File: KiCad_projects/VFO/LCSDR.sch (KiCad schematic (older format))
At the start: 78 parts, among them J1 SPI, J10 ENCODER, J11 LCD, J12 keyboard, J2 BAND, J3 OUT-TX, J4 UART, J5 PA, J6 12v, J7 OUT 1-120Mhz, J8 ATT, J9 PRE, Q1 MMBT2907, Q2 MMBT2222, Q3 MMBT2907, U1 ATMEGA328P-AU, U2 Si5351, U3 PCA9306, U4 ADuM1201BR, U5 LD1117S50TR, U6 LD1117S33TR, Y1 16Mhz, Y2 25Mhz

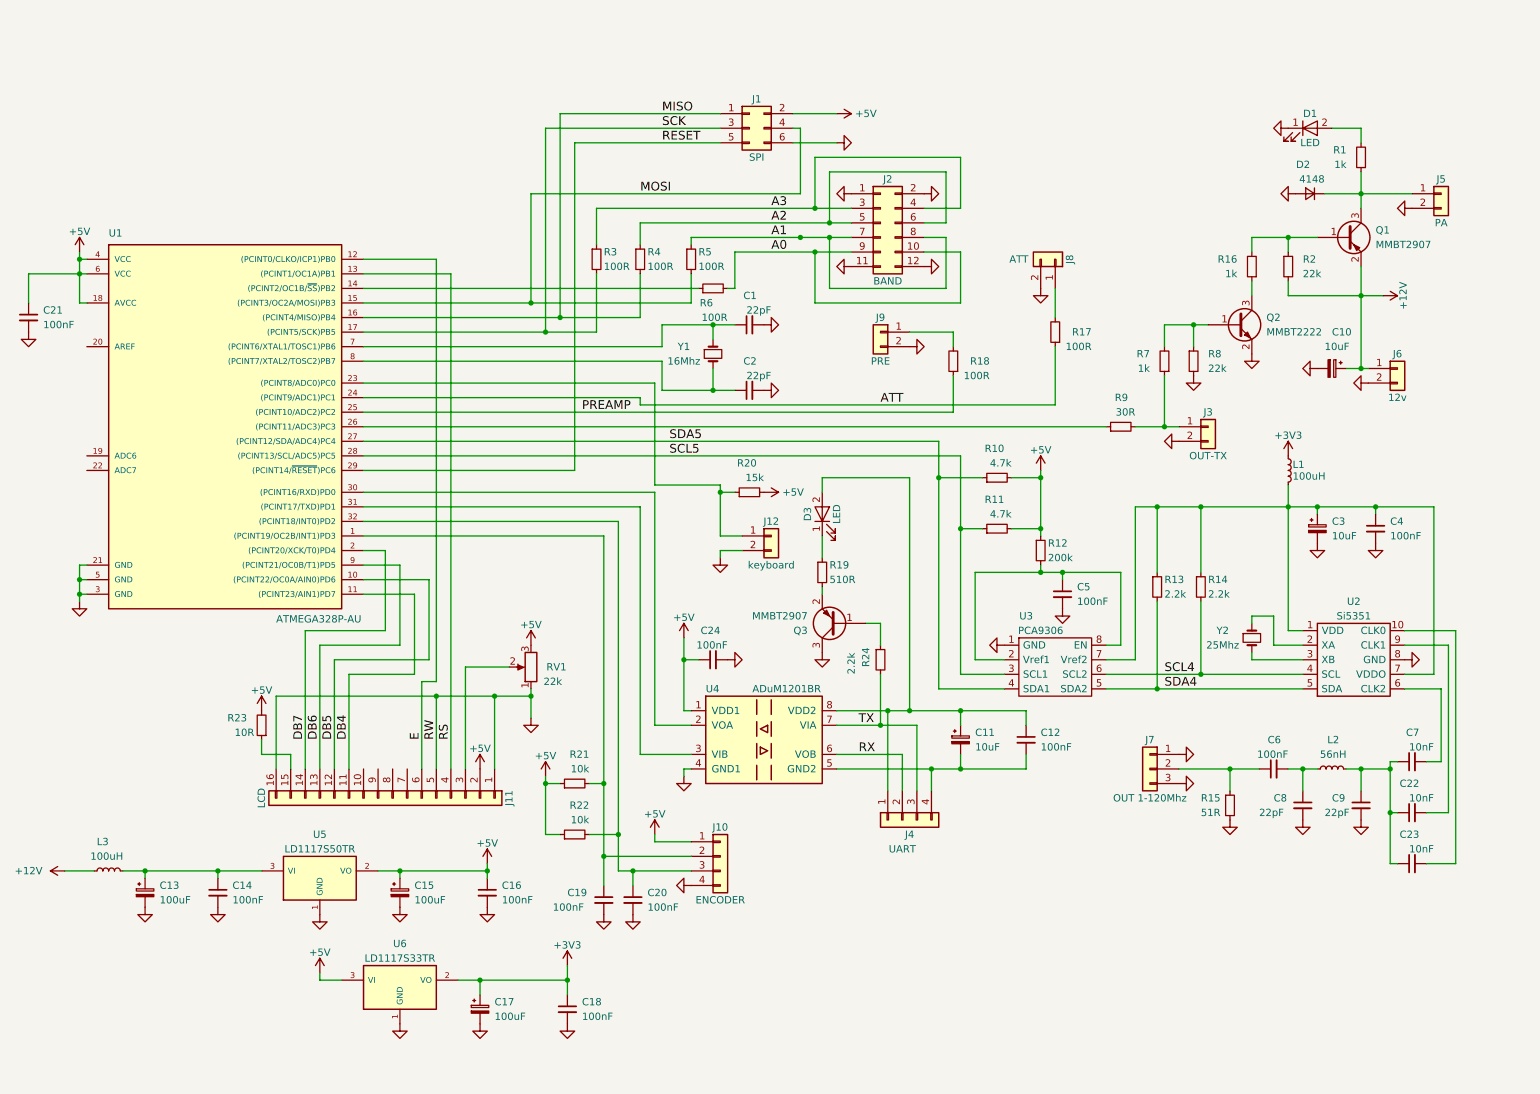
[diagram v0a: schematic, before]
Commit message: modified VFO schematics and PCB. clk0/clk1/clk2, unified management board
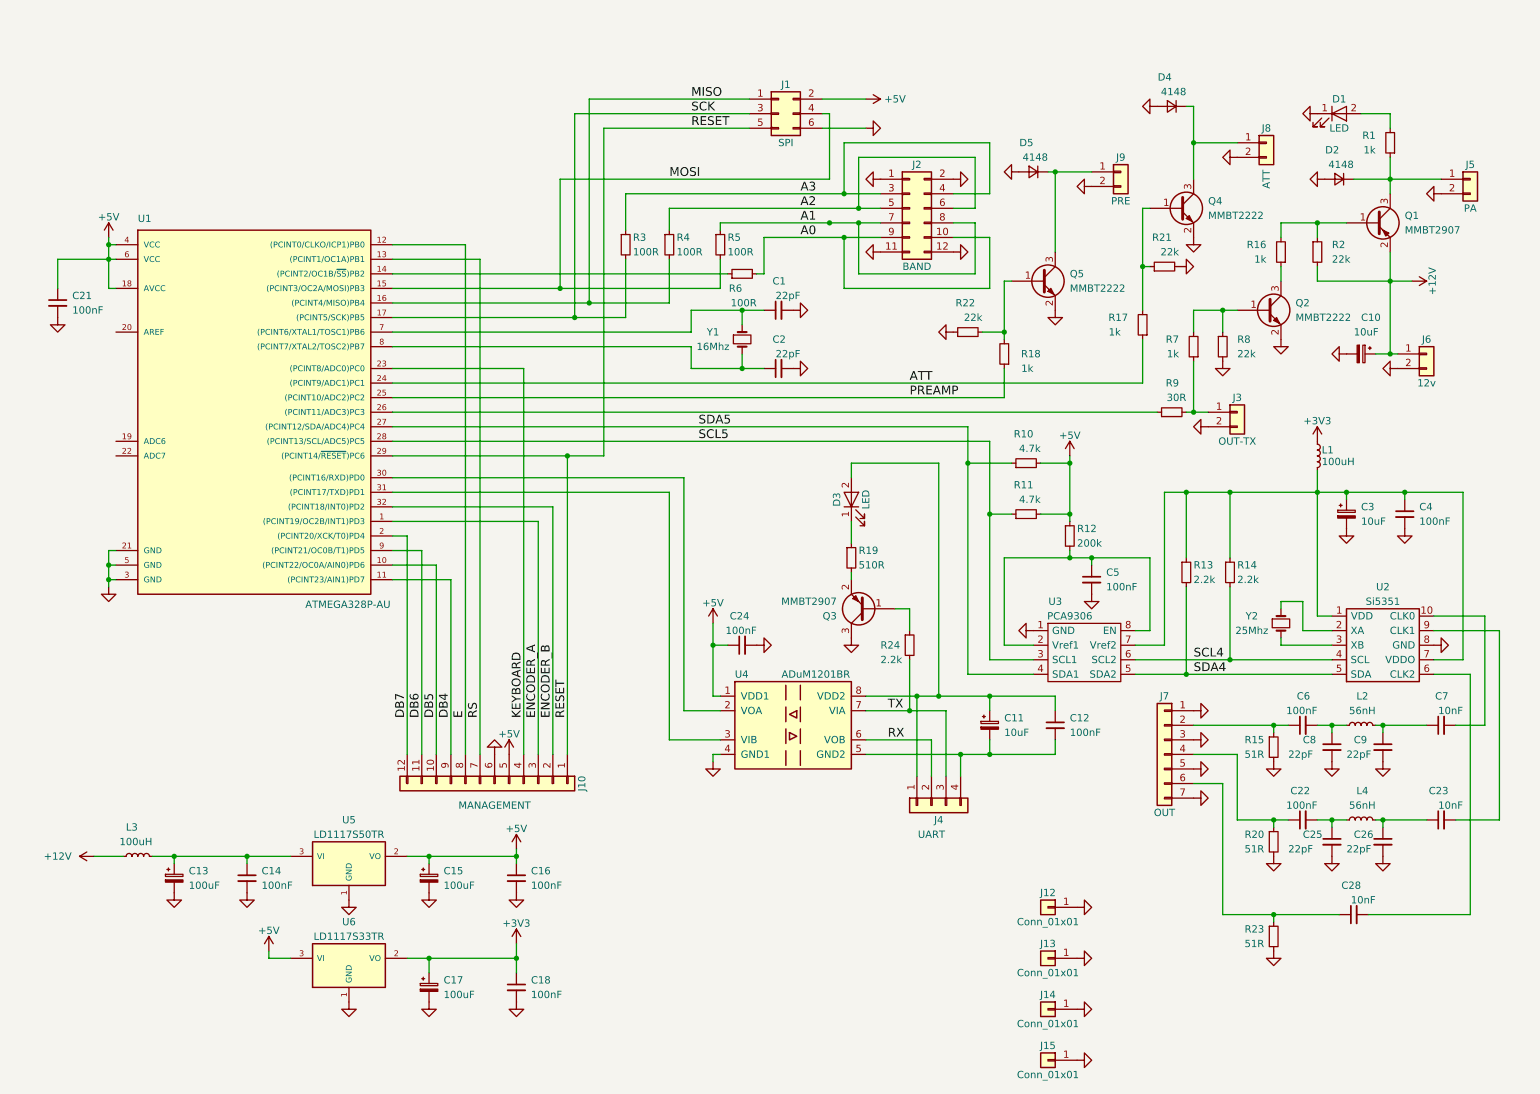
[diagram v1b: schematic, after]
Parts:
- removed C19, C20: 100nF, LCSDR:C_1206_0603, symbol C_Small
- removed J10: ENCODER, Pin_Headers:Pin_Header_Angled_1x04_Pitch2.54mm, symbol Conn_01x04
- removed J11: LCD, Pin_Headers:Pin_Header_Angled_1x16_Pitch2.54mm, symbol Conn_01x16
- removed J12: keyboard, Pin_Headers:Pin_Header_Angled_1x02_Pitch2.54mm, symbol Conn_01x02
- removed J7: OUT 1-120Mhz, Pin_Headers:Pin_Header_Straight_1x03_Pitch2.54mm, symbol Conn_01x03
- removed RV1: 22k, Potentiometers:Potentiometer_Trimmer_Piher_PT-6v_Horizontal, symbol POT
- added C25, C26: 22pF, LCSDR:C_1206_0603, symbol C_Small
- added C28: 10nF, LCSDR:C_1206_0603, symbol C_Small
- added D4, D5: 4148, Diodes_SMD:D_MiniMELF_Handsoldering, symbol D_Small
- added J10: MANAGEMENT, Pin_Headers:Pin_Header_Angled_1x12_Pitch2.54mm, symbol Conn_01x12
- added J12, J13, J14, J15: Conn_01x01, Mounting_Holes:MountingHole_3.2mm_M3_DIN965_Pad, symbol Conn_01x01
- added J7: OUT, Pin_Headers:Pin_Header_Straight_1x07_Pitch2.54mm, symbol Conn_01x07
- added L4: 56nH, LCSDR:C_1206_0603, symbol L_Small
- added Q4, Q5: MMBT2222, TO_SOT_Packages_SMD:SOT-23W_Handsoldering, symbol Q_NPN_BEC
- C22: value 10nF -> 100nF
- L2: footprint Capacitors_SMD:C_0603_HandSoldering -> LCSDR:C_1206_0603
- R17, R18: value 100R -> 1k
- R20: value 15k -> 51R
- R21, R22: value 10k -> 22k
- R23: value 10R -> 51R
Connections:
- net +5V: now also J10.5 (Pin_5); no longer R20.2, R21.1, R22.1, R23.2
- net DB4: now also J10.9 (Pin_9)
- net DB5: now also J10.10 (Pin_10)
- net DB6: now also J10.11 (Pin_11)
- net DB7: now also J10.12 (Pin_12)
- net E: now also J10.8 (Pin_8)
- net GND: now also R20.2, R21.2, R22.1, R23.2, C25.2, C26.2, D4.2 (A), D5.2 (A), J10.6 (Pin_6), J12.1 (Pin_1), J13.1 (Pin_1), J14.1 (Pin_1), J15.1 (Pin_1), J7.1 (Pin_1), J7.3 (Pin_3), J7.5 (Pin_5), J7.7 (Pin_7), Q4.2 (E), Q5.2 (E)
- net RESET: now also J10.1 (Pin_1)
- net RS: now also J10.7 (Pin_7)
- net ENCODER_A: now reaches U1.1 ((PCINT19/OC2B/INT1)PD3)
- net ENCODER_A: now also J10.3 (Pin_3); no longer R21.2
- net at R20.1: now also C22.1, J7.4 (Pin_4); no longer U1.23 ((PCINT8/ADC0)PC0)
- net at R22.2: now also R18.2, Q5.1 (B); no longer U1.32 ((PCINT18/INT0)PD2)
- net at U2.10 (CLK0): now also C7.2; no longer C23.2
- net at U2.6 (CLK2): now also C28.2; no longer C7.2
- net at U2.9 (CLK1): now also C23.2; no longer C22.2
- net at C7.1, C9.1, L2.2: no longer C22.1, C23.1
- net at C6.1, R15.1: now also J7.2 (Pin_2)
- net at R23.1: now also C28.1, J7.6 (Pin_6)
- net at J9.1 (Pin_1): now also D5.1 (K), Q5.3 (C); no longer R18.2
- net at R17.2: now also R21.1, Q4.1 (B); no longer J8.1 (Pin_1)
- new net: D4.1 (K), J8.1 (Pin_1), Q4.3 (C)
- new net: C23.1, C26.1, L4.2
- new net: C22.2, C25.1, L4.1
- new net ENCODER_B: J10.2 (Pin_2), U1.32 ((PCINT18/INT0)PD2)
- new net KEYBOARD: J10.4 (Pin_4), U1.23 ((PCINT8/ADC0)PC0)
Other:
- moved on the sheet: C1, C10, C11, C12, C13, C14, C15, C16, C17, C18, C2, C21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

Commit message: Separate boards for VFO, CLK0, CLK1, CLK2 and SWR
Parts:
- added C19, C20: 100nF, LCSDR:C_1206_0603, symbol C_Small
- added J11: Conn_01x03, Pin_Headers:Pin_Header_Angled_1x03_Pitch2.54mm, symbol Conn_01x03
- added R25, R26, R27, R28: 2.2k, LCSDR:R_1206_0603, symbol R_Small
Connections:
- net GND: now also C19.1, C20.1, J11.3 (Pin_3), R25.2, R26.2
- net at U1.19 (ADC6): now also C19.2, R25.1, R28.1
- net at U1.22 (ADC7): now also C20.2, R26.1, R27.1
- new net: J11.1 (Pin_1), R28.2
- new net: J11.2 (Pin_2), R27.2
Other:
- moved on the sheet: C1, C10, C11, C12, C13, C14, C15, C16, C17, C18, C2, C21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

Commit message: Fix some small issues and first tantal release
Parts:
- C10, C11, C3: footprint Capacitors_ThroughHole:CP_Radial_D5.0mm_P2.00mm -> Capacitors_Tantalum_SMD:CP_Tantalum_Case-A_EIA-3216-18_Hand
- C13, C15, C17: footprint Capacitors_ThroughHole:CP_Radial_D6.3mm_P2.50mm -> Capacitors_Tantalum_SMD:CP_Tantalum_Case-D_EIA-7343-31_Hand

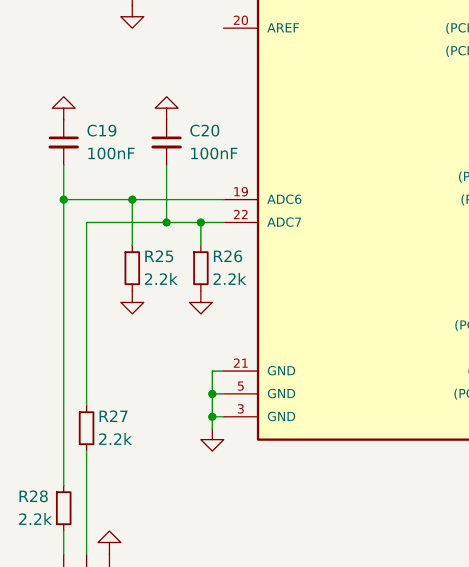
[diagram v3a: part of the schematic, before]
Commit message: Fix Issues with PCB Silk Text
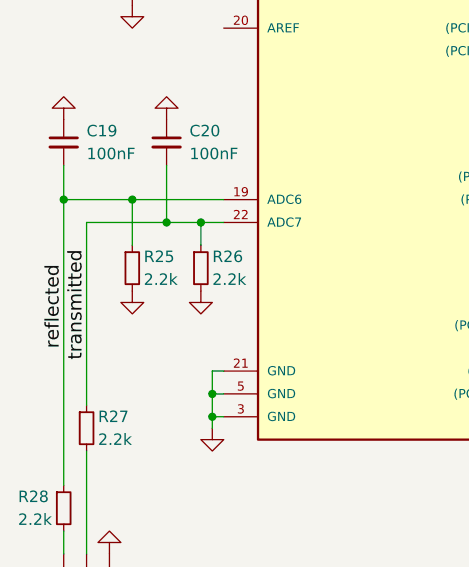
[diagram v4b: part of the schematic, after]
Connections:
- net reflected: now reaches C19.2, R25.1, R28.1, U1.19 (ADC6)
- net transmitted: now reaches C20.2, R26.1, R27.1, U1.22 (ADC7)
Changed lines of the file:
@@
 Sheet 1 1
 Title "ut3mk"
-Date "2017-12-29"
-Rev "1.04"
+Date "2018-01-01"
+Rev "1.05"
 Comp ""
 Comment1 "Vasyl Kuzmenko"
@@
 	-1   0    0    1
 $EndComp
+Text Label 700  3650 1    60   ~ 0
+reflected
+Text Label 800  3700 1    60   ~ 0
+transmitted
 $EndSCHEMATC
